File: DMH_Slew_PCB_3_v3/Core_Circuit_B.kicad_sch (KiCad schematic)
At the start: 60 parts, among them J21 Conn_02x03_Top_Bottom, J22 Conn_02x06_Top_Bottom, J23 Conn_02x03_Top_Bottom, J24 Conn_02x03_Top_Bottom, J25 Conn_02x06_Top_Bottom, J26 Conn_02x03_Top_Bottom, J27 Conn_01x08, J28 Conn_01x08, J29 Conn_01x08, J30 Conn_01x08, J6 TS_Jack_6.35mm_Sw, J7 TS_Jack_6.35mm_Sw, J8 TS_Jack_6.35mm_Sw, Q10 BC558, Q7 BC548, Q8 BC548, Q9 BC558, SW4 SW_DPDT_3way, SW5 SW_DPDT, SW6 SPDT_OnOffOn, U3 TL074, U4 TL074

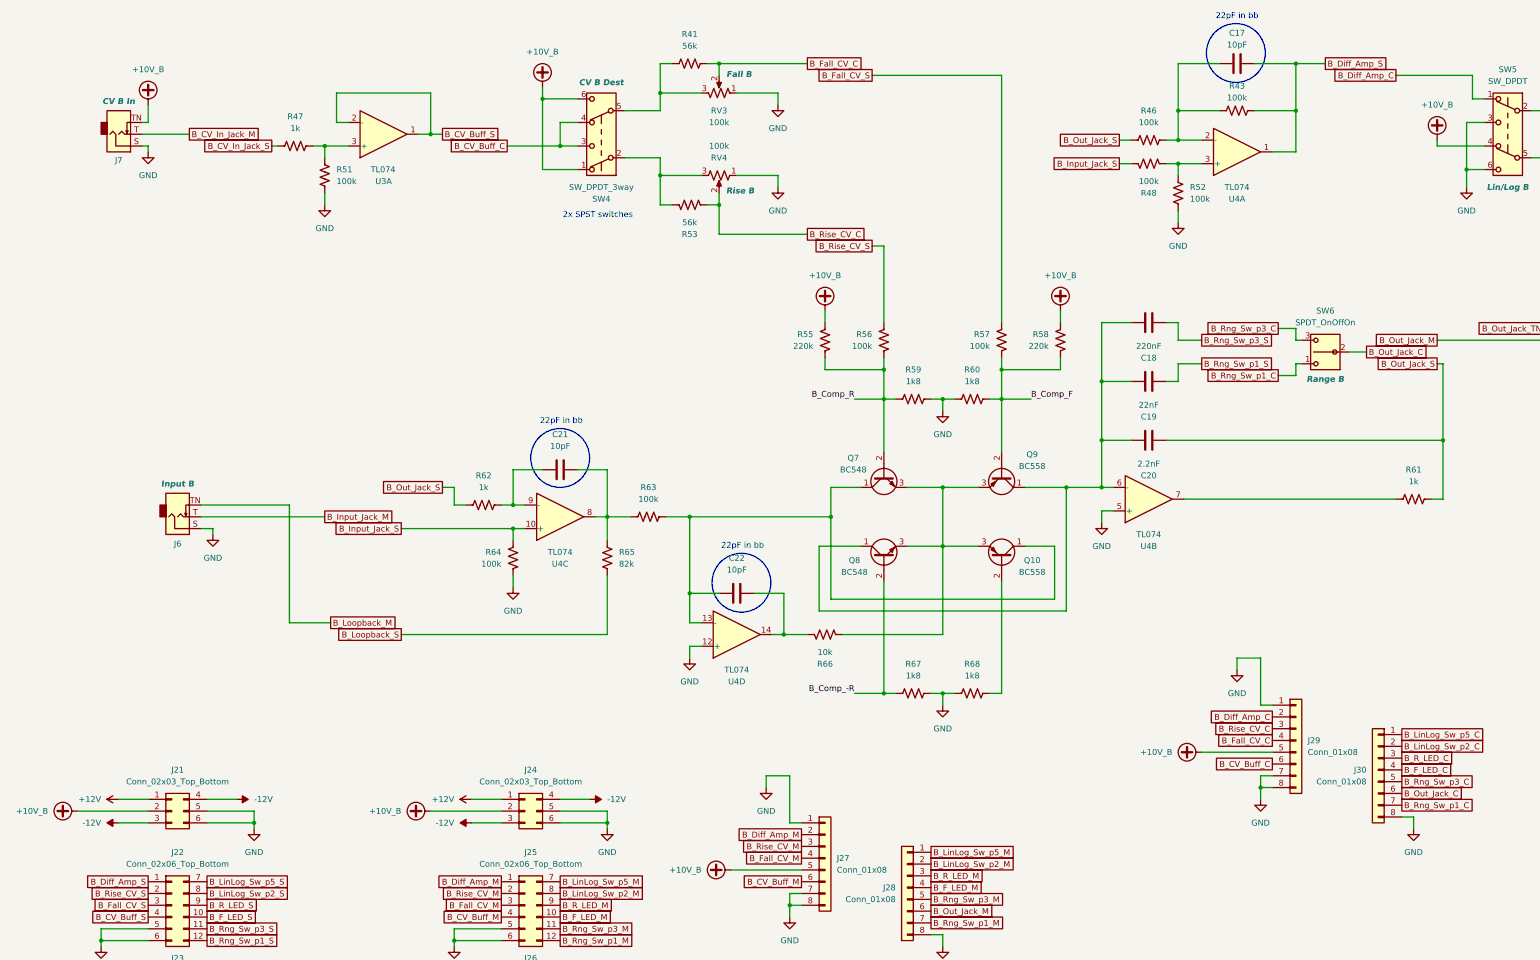
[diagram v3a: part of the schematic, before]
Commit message: Redesigned Main PCB
and regenerated Gerbers
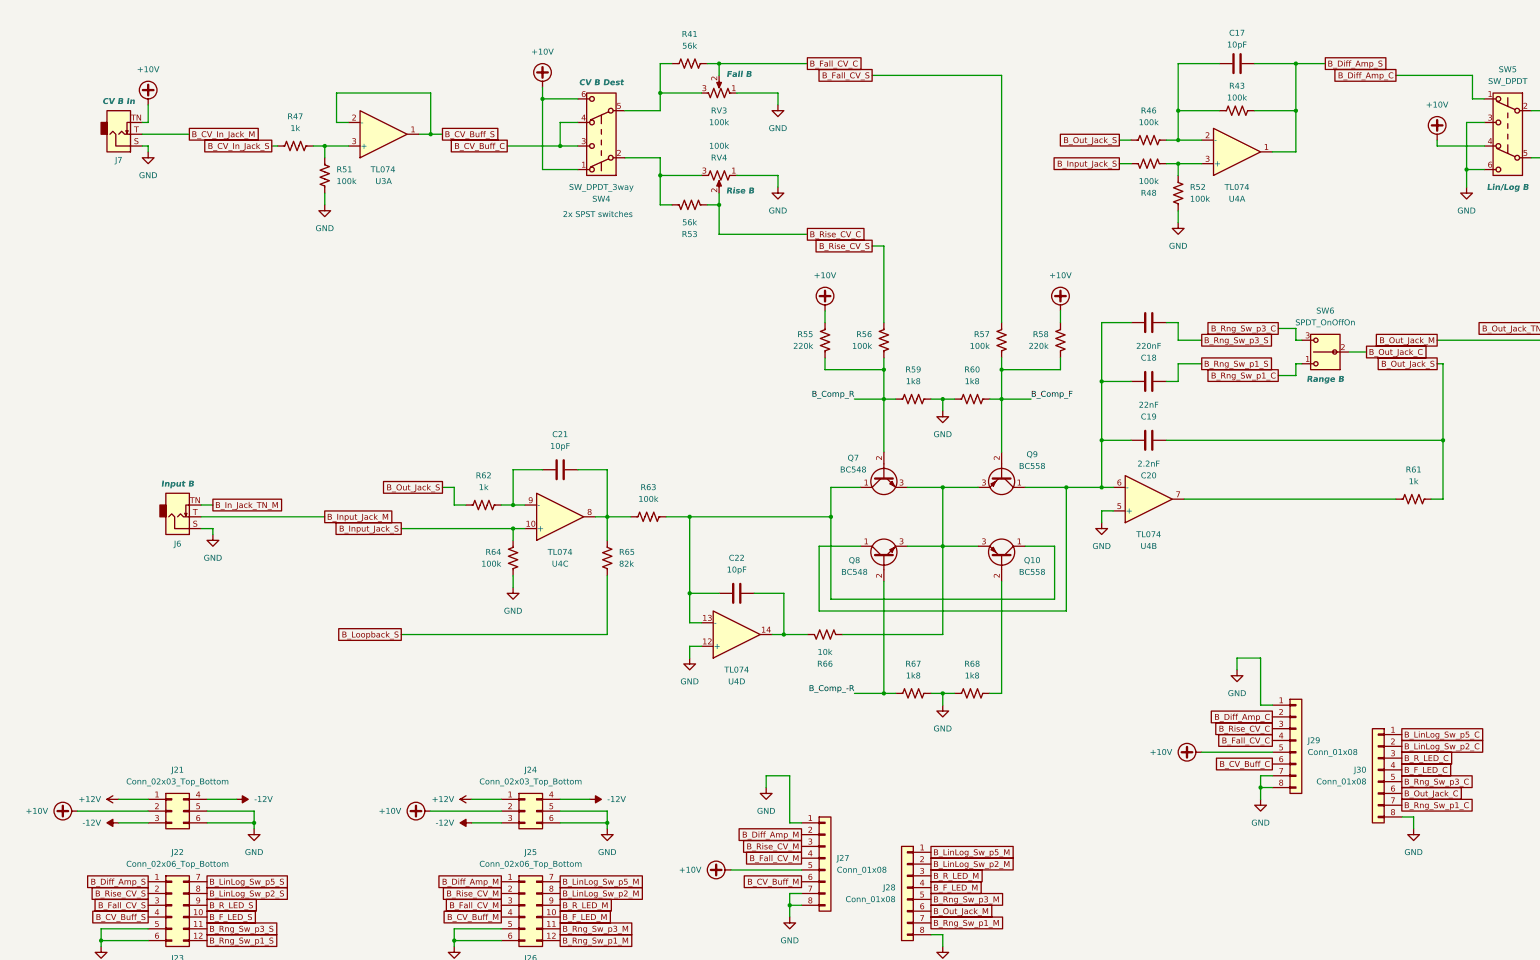
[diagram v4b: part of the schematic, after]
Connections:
- net B_Loopback_M: no longer J6.TN
- net +10V_B renamed +10V
- new net B_In_Jack_TN_M: J6.TN
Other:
- note removed: "22pF in bb"
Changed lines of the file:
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@@
 		(comment 1 "PCB for 5 cm Kosmo format synthesizer module")
 	)
-	(circle
-		(center 279.146 65.024)
-		(radius 6.35)
-		(stroke
-			(width 0)
-			(type default)
-		)
-		(fill
-			(type none)
-		)
-	)
-	(circle
-		(center 172.466 179.324)
-		(radius 6.35)
-		(stroke
-			(width 0)
-			(type default)
-		)
-		(fill
-			(type none)
-		)
-	)
-	(circle
-		(center 133.35 152.4)
-		(radius 6.35)
-		(stroke
-			(width 0)
-			(type default)
-		)
-		(fill
-			(type none)
-		)
-	)
-	(text "22pF in bb"
-		(exclude_from_sim no)
-		(at 172.72 171.45 0)
-		(effects
-			(font
-				(size 1.27 1.27)
-			)
-		)
-	)
-	(text "22pF in bb"
-		(exclude_from_sim no)
-		(at 133.604 144.526 0)
-		(effects
-			(font
-				(size 1.27 1.27)
-			)
-		)
-	)
 	(text "2x SPST switches"
 		(exclude_from_sim no)
@@
 		)
 	)
-	(text "22pF in bb"
-		(exclude_from_sim no)
-		(at 279.4 57.15 0)
-		(effects
-			(font
-				(size 1.27 1.27)
-			)
-		)
-	)
 	(junction
 		(at 228.6 139.7)
@@
 	(wire
 		(pts
-			(xy 74.93 162.56) (xy 74.93 187.96)
+			(xy 147.32 87.63) (xy 154.94 87.63)
 		)
 		(stroke
@@
 	(wire
 		(pts
-			(xy 147.32 87.63) (xy 154.94 87.63)
+			(xy 241.3 120.65) (xy 241.3 123.19)
 		)
 		(stroke
@@
 	(wire
 		(pts
-			(xy 241.3 120.65) (xy 241.3 123.19)
+			(xy 342.9 87.63) (xy 349.25 87.63)
 		)
 		(stroke
@@
 	(wire
 		(pts
-			(xy 342.9 87.63) (xy 349.25 87.63)
+			(xy 58.42 167.64) (xy 55.88 167.64)
 		)
 		(stroke
@@
 	(wire
 		(pts
-			(xy 58.42 167.64) (xy 55.88 167.64)
+			(xy 161.29 181.61) (xy 167.64 181.61)
 		)
 		(stroke
@@
 	(wire
 		(pts
-			(xy 161.29 181.61) (xy 167.64 181.61)
+			(xy 55.88 162.56) (xy 58.42 162.56)
 		)
 		(stroke
@@
 	(wire
 		(pts
-			(xy 55.88 162.56) (xy 74.93 162.56)
-		)
-		(stroke
-			(width 0)
-			(type default)
-		)
-	)
-	(wire
-		(pts
 			(xy 288.29 134.62) (xy 292.1 134.62)
 		)
@@
 	(wire
 		(pts
-			(xy 74.93 187.96) (xy 83.82 187.96)
-		)
-		(stroke
-			(width 0)
-			(type default)
-		)
-	)
-	(wire
-		(pts
 			(xy 323.85 132.08) (xy 323.85 148.59)
 		)
@@
 		)
 	)
+	(global_label "B_In_Jack_TN_M"
+		(shape passive)
+		(at 58.42 162.56 0)
+		(fields_autoplaced yes)
+		(effects
+			(font
+				(size 1.27 1.27)
+			)
+			(justify left)
+		)
+		(property "Intersheetrefs" "${INTERSHEET_REFS}"
+			(at 75.1709 162.56 0)
+			(effects
+				(font
+					(size 1.27 1.27)
+				)
+				(justify left)
+				(hide yes)
+			)
+		)
+	)
 	(global_label "B_CV_Buff_C"
 		(shape passive)
@@
 		)
 	)
-	(global_label "B_Loopback_M"
-		(shape passive)
-		(at 83.82 187.96 0)
-		(fields_autoplaced yes)
-		(effects
-			(font
-				(size 1.27 1.27)
-			)
-			(justify left)
-		)
-		(property "Intersheetrefs" "${INTERSHEET_REFS}"
-			(at 99.2403 187.96 0)
-			(effects
-				(font
-					(size 1.27 1.27)
-				)
-				(justify left)
-				(hide yes)
-			)
-		)
-	)
 	(global_label "B_Rng_Sw_p1_S"
 		(shape passive)
@@
 			)
 		)
-		(property "Value" "+10V_B"
+		(property "Value" "+10V"
 			(at 190.5 113.03 0)
 			(effects
@@
 			)
 		)
-		(property "Value" "+10V_B"
+		(property "Value" "+10V"
 			(at 322.58 76.2 0)
 			(effects
@@
 			)
 		)
-		(property "Value" "+10V_B"
+		(property "Value" "+10V"
 			(at 265.43 215.8999 90)
 			(effects
@@
 			)
 		)
-		(property "Value" "+10V_B"
+		(property "Value" "+10V"
 			(at 163.83 241.2999 90)
 			(effects
@@
 			)
 		)
-		(property "Value" "+10V_B"
+		(property "Value" "+10V"
 			(at 241.3 113.03 0)
 			(effects
@@
 			)
 		)
-		(property "Value" "+10V_B"
+		(property "Value" "+10V"
 			(at 22.86 228.5999 90)
 			(effects
@@
 			)
 		)
-		(property "Value" "+10V_B"
+		(property "Value" "+10V"
 			(at 129.54 64.77 0)
 			(effects
@@
 			)
 		)
-		(property "Value" "+10V_B"
+		(property "Value" "+10V"
 			(at 44.45 68.58 0)
 			(effects
@@
 	)
 	(symbol
-		(lib_name "Switch_DPDT_1")
 		(lib_id "SynthStuff:Switch_DPDT")
 		(at 142.24 82.55 180)
@@
 			)
 		)
-		(property "Value" "+10V_B"
+		(property "Value" "+10V"
 			(at 99.06 228.5999 90)
 			(effects

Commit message: Cleaned up old breadboarding notes
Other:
- note removed: "2x SPST switches"
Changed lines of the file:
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@@
 		(comment 1 "PCB for 5 cm Kosmo format synthesizer module")
-	)
-	(text "2x SPST switches"
-		(exclude_from_sim no)
-		(at 141.478 100.076 0)
-		(effects
-			(font
-				(size 1.27 1.27)
-			)
-		)
 	)
 	(junction
